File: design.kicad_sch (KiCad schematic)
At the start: 80 parts, among them J1 2601-3108, J10 Conn_01x04, J11 Conn_01x04, J12 Conn_01x03, J13 Conn_01x03, J14 BM04B-SRSS-TB_LF__SN_, J2 2601-3108, J3 2601-3108, J4 TYPE-C-31-M-12, J5 SKEDD-UPDI-4, J6 Conn_01x04, J7 Conn_01x04, J8 Conn_01x04, J9 Conn_01x04, U1 ATtiny1616-S, U2 AP2112K-3.3, U3 CP2105

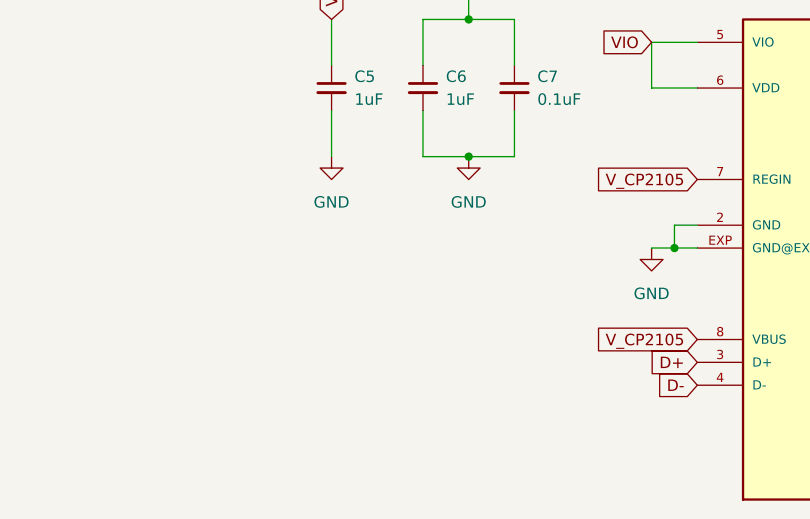
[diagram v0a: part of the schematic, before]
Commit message: add CP2105 VBus solderbridge
closes #5
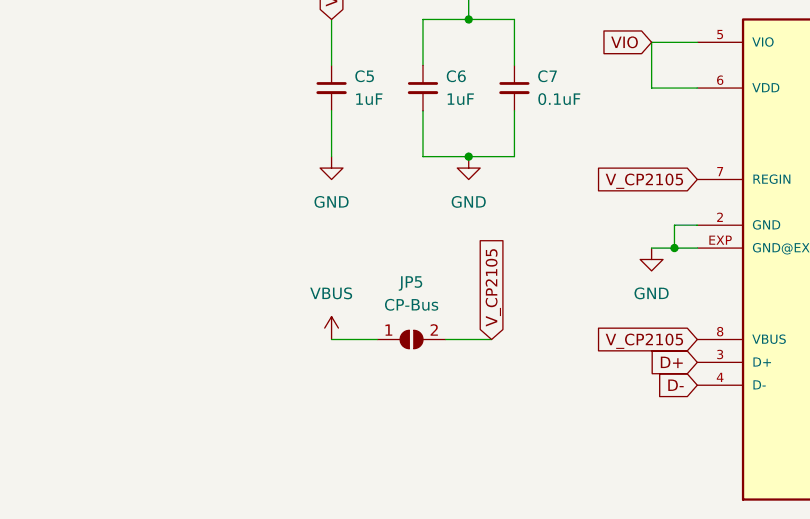
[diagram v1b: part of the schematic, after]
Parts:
- added JP5: CP-Bus, Jumper:SolderJumper-2_P1.3mm_Open_Pad1.0x1.5mm, symbol Jumper:SolderJumper_2_Open
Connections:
- net VBUS: now also JP5.1 (A)
- net V_CP2105: now also JP5.2 (B)
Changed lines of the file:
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@@
     (stroke (width 0) (type default) (color 0 0 0 0))
   )
+  (wire (pts (xy 175.26 248.92) (xy 180.34 248.92))
+    (stroke (width 0) (type default) (color 0 0 0 0))
+  )
   (wire (pts (xy 358.14 185.42) (xy 358.14 180.34))
     (stroke (width 0) (type default) (color 0 0 0 0))
@@
     (stroke (width 0) (type default) (color 0 0 0 0))
   )
+  (wire (pts (xy 162.56 248.92) (xy 167.64 248.92))
+    (stroke (width 0) (type default) (color 0 0 0 0))
+  )
   (wire (pts (xy 28.575 33.02) (xy 33.02 33.02))
     (stroke (width 0) (type default) (color 0 0 0 0))
@@
     )
   )
+  (global_label "V_CP2105" (shape input) (at 180.34 248.92 90) (fields_autoplaced)
+    (effects (font (size 1.27 1.27)) (justify left))
+    (property "Referenzen zwischen Schaltplänen" "${INTERSHEET_REFS}" (id 0) (at 180.2606 237.1615 90)
+      (effects (font (size 1.27 1.27)) (justify left) hide)
+    )
+  )
   (global_label "PB0" (shape input) (at 96.52 150.749 180) (fields_autoplaced)
     (effects (font (size 1.27 1.27)) (justify right))
@@
     (pin "4")
   )
+  (symbol (lib_id "Jumper:SolderJumper_2_Open") (at 171.45 248.92 0) (unit 1)
+    (in_bom yes) (on_board yes) (fields_autoplaced)
+    (property "Reference" "JP5" (id 0) (at 171.45 242.57 0))
+    (property "Value" "CP-Bus" (id 1) (at 171.45 245.11 0))
+    (property "Footprint" "Jumper:SolderJumper-2_P1.3mm_Open_Pad1.0x1.5mm" (id 2) (at 171.45 248.92 0)
+      (effects (font (size 1.27 1.27)) hide)
+    )
+    (property "Datasheet" "~" (id 3) (at 171.45 248.92 0)
+      (effects (font (size 1.27 1.27)) hide)
+    )
+    (pin "1")
+    (pin "2")
+  )
   (symbol (lib_id "power:PWR_FLAG") (at 237.49 154.94 90) (unit 1)
     (in_bom yes) (on_board yes)
@@
     (pin "1")
   )
+  (symbol (lib_id "power:VBUS") (at 162.56 248.92 0) (unit 1)
+    (in_bom yes) (on_board yes) (fields_autoplaced)
+    (property "Reference" "#PWR0106" (id 0) (at 162.56 252.73 0)
+      (effects (font (size 1.27 1.27)) hide)
+    )
+    (property "Value" "VBUS" (id 1) (at 162.56 243.84 0))
+    (property "Footprint" "" (id 2) (at 162.56 248.92 0)
+      (effects (font (size 1.27 1.27)) hide)
+    )
+    (property "Datasheet" "" (id 3) (at 162.56 248.92 0)
+      (effects (font (size 1.27 1.27)) hide)
+    )
+    (pin "1")
+  )
   (symbol (lib_id "power:VBUS") (at 167.64 157.48 0) (mirror y) (unit 1)
     (in_bom yes) (on_board yes)
@@
       (reference "#PWR0105") (unit 1) (value "VCC") (footprint "")
     )
+    (path "/528fa40b-d5ff-4783-ba33-55bca0f34b24"
+      (reference "#PWR0106") (unit 1) (value "VBUS") (footprint "")
+    )
     (path "/c097fc70-84bb-4a84-8a27-d6457ac14a2c"
       (reference "#PWR0107") (unit 1) (value "GND") (footprint "")
@@
       (reference "JP4") (unit 1) (value "LED2x2") (footprint "Jumper:SolderJumper-2_P1.3mm_Open_Pad1.0x1.5mm")
     )
+    (path "/14405b68-8ab5-4c92-8056-b559eb773953"
+      (reference "JP5") (unit 1) (value "CP-Bus") (footprint "Jumper:SolderJumper-2_P1.3mm_Open_Pad1.0x1.5mm")
+    )
     (path "/be5d4d29-c7d2-4c92-a91e-3f85187a2fa5"

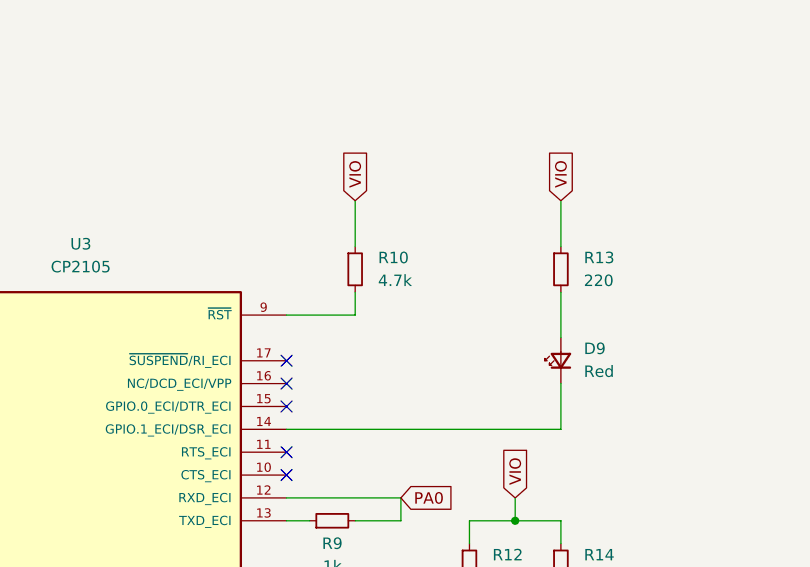
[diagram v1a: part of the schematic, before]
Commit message: add programming capacitor
closes #4
to use the TX/RX LEDs the cp2105 must be programmed to use this function (only one time possible). Todo this a 4,7uF capacitor must be used on pin VPP according to the Datasheet Note 4 page 18.
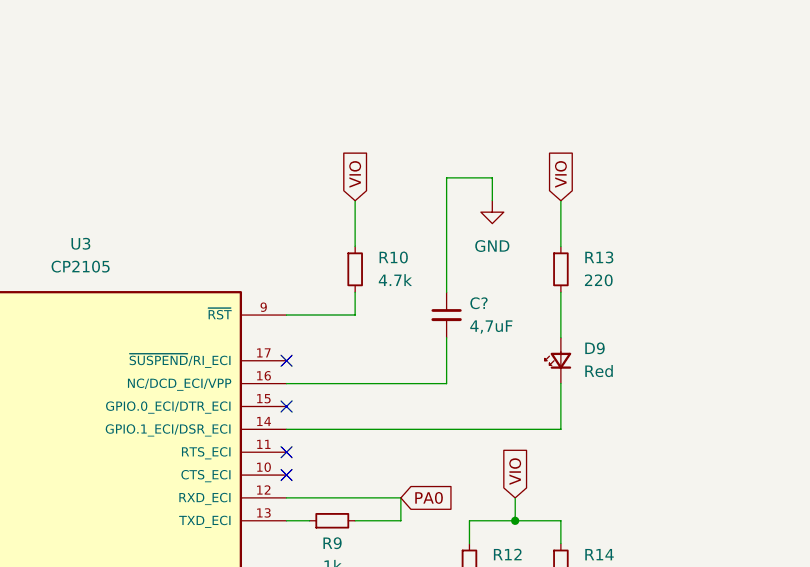
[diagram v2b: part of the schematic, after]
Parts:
- added C?: 4,7uF, Capacitor_SMD:C_0805_2012Metric, symbol Device:C_Small
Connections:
- net GND: now also C?.1
- net at U3.16 (NC/DCD_ECI/VPP): now also C?.2
- no-connect marks 14 -> 13
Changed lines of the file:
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@@
   )
   (no_connect (at 248.92 220.98))
-  (no_connect (at 248.92 223.52))
   (no_connect (at 248.92 233.68))
   (no_connect (at 68.58 45.72))
@@
     (stroke (width 0) (type default) (color 0 0 0 0))
   )
+  (wire (pts (xy 266.7 200.66) (xy 266.7 213.36))
+    (stroke (width 0) (type default) (color 0 0 0 0))
+  )
   (wire (pts (xy 71.12 182.88) (xy 71.12 180.34))
     (stroke (width 0) (type default) (color 0 0 0 0))
@@
     (stroke (width 0) (type default) (color 0 0 0 0))
   )
+  (wire (pts (xy 266.7 223.52) (xy 266.7 218.44))
+    (stroke (width 0) (type default) (color 0 0 0 0))
+  )
   (wire (pts (xy 358.14 205.74) (xy 358.14 200.66))
     (stroke (width 0) (type default) (color 0 0 0 0))
@@
     (stroke (width 0) (type default) (color 0 0 0 0))
   )
+  (wire (pts (xy 271.78 200.66) (xy 266.7 200.66))
+    (stroke (width 0) (type default) (color 0 0 0 0))
+  )
   (wire (pts (xy 322.58 144.78) (xy 325.12 144.78))
     (stroke (width 0) (type default) (color 0 0 0 0))
@@
     (stroke (width 0) (type default) (color 0 0 0 0))
   )
+  (wire (pts (xy 248.92 223.52) (xy 266.7 223.52))
+    (stroke (width 0) (type default) (color 0 0 0 0))
+  )
   (wire (pts (xy 172.085 40.64) (xy 180.34 40.64))
     (stroke (width 0) (type default) (color 0 0 0 0))
@@
     (stroke (width 0) (type default) (color 0 0 0 0))
   )
+  (wire (pts (xy 271.78 203.2) (xy 271.78 200.66))
+    (stroke (width 0) (type default) (color 0 0 0 0))
+  )
   (wire (pts (xy 353.06 139.7) (xy 353.06 137.16))
     (stroke (width 0) (type default) (color 0 0 0 0))
@@
     (pin "1")
   )
+  (symbol (lib_id "power:GND") (at 271.78 203.2 0) (unit 1)
+    (in_bom yes) (on_board yes) (fields_autoplaced)
+    (property "Reference" "#PWR?" (id 0) (at 271.78 209.55 0)
+      (effects (font (size 1.27 1.27)) hide)
+    )
+    (property "Value" "GND" (id 1) (at 271.78 208.28 0))
+    (property "Footprint" "" (id 2) (at 271.78 203.2 0)
+      (effects (font (size 1.27 1.27)) hide)
+    )
+    (property "Datasheet" "" (id 3) (at 271.78 203.2 0)
+      (effects (font (size 1.27 1.27)) hide)
+    )
+    (pin "1")
+  )
   (symbol (lib_id "power:VDD") (at 355.6 83.82 0) (mirror y) (unit 1)
     (in_bom yes) (on_board yes)
@@
     (pin "1")
   )
+  (symbol (lib_id "Device:C_Small") (at 266.7 215.9 0) (unit 1)
+    (in_bom yes) (on_board yes) (fields_autoplaced)
+    (property "Reference" "C?" (id 0) (at 269.24 214.6362 0)
+      (effects (font (size 1.27 1.27)) (justify left))
+    )
+    (property "Value" "4,7uF" (id 1) (at 269.24 217.1762 0)
+      (effects (font (size 1.27 1.27)) (justify left))
+    )
+    (property "Footprint" "Capacitor_SMD:C_0805_2012Metric" (id 2) (at 266.7 215.9 0)
+      (effects (font (size 1.27 1.27)) hide)
+    )
+    (property "Datasheet" "~" (id 3) (at 266.7 215.9 0)
+      (effects (font (size 1.27 1.27)) hide)
+    )
+    (pin "1")
+    (pin "2")
+  )
   (symbol (lib_id "power:GND") (at 18.796 170.18 0) (unit 1)
     (in_bom yes) (on_board yes)
@@
       (reference "#PWR0189") (unit 1) (value "GND") (footprint "")
     )
+    (path "/cc5fd905-24ad-457d-947c-2c2437ded00b"
+      (reference "#PWR?") (unit 1) (value "GND") (footprint "")
+    )
     (path "/5005112b-a25c-4019-a0f7-bec67dd371e4"
       (reference "C1") (unit 1) (value "1uF") (footprint "Capacitor_SMD:C_0805_2012Metric")
@@
       (reference "C7") (unit 1) (value "0.1uF") (footprint "Capacitor_SMD:C_0805_2012Metric")
     )
+    (path "/d80388e9-556a-442b-9d58-9f39d8934e6e"
+      (reference "C?") (unit 1) (value "4,7uF") (footprint "Capacitor_SMD:C_0805_2012Metric")
+    )
     (path "/5ec38a02-a145-4acb-a554-76dbb10c2abb"

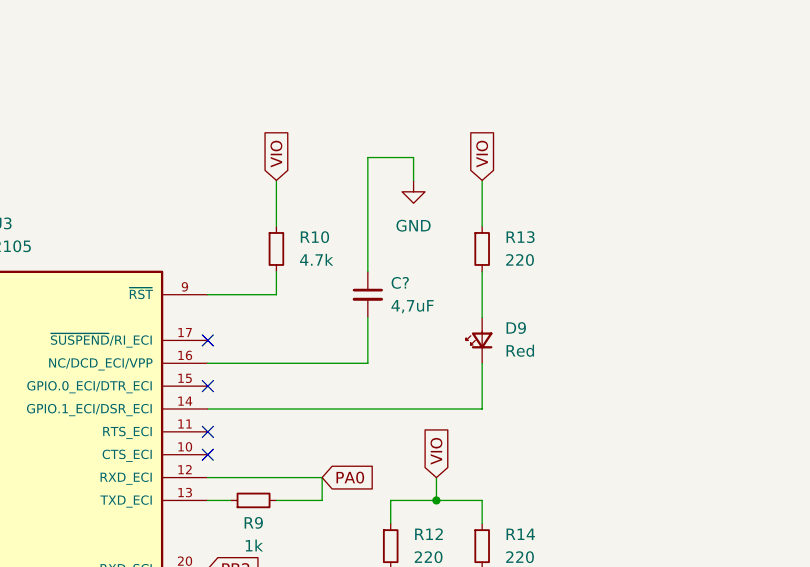
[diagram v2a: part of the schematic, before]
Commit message: add designators
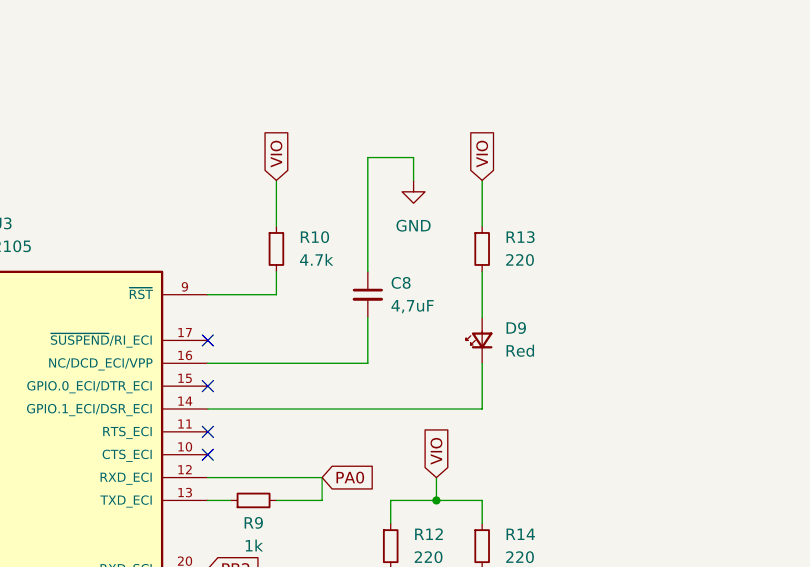
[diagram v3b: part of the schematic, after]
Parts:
- gave numbers to parts that had none: 1
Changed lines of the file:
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@@
   (symbol (lib_id "power:GND") (at 271.78 203.2 0) (unit 1)
     (in_bom yes) (on_board yes) (fields_autoplaced)
-    (property "Reference" "#PWR?" (id 0) (at 271.78 209.55 0)
+    (property "Reference" "#PWR0190" (id 0) (at 271.78 209.55 0)
       (effects (font (size 1.27 1.27)) hide)
     )
@@
   (symbol (lib_id "Device:C_Small") (at 266.7 215.9 0) (unit 1)
     (in_bom yes) (on_board yes) (fields_autoplaced)
-    (property "Reference" "C?" (id 0) (at 269.24 214.6362 0)
+    (property "Reference" "C8" (id 0) (at 269.24 214.6362 0)
       (effects (font (size 1.27 1.27)) (justify left))
     )
@@
     )
     (path "/cc5fd905-24ad-457d-947c-2c2437ded00b"
-      (reference "#PWR?") (unit 1) (value "GND") (footprint "")
+      (reference "#PWR0190") (unit 1) (value "GND") (footprint "")
     )
     (path "/5005112b-a25c-4019-a0f7-bec67dd371e4"
@@
     )
     (path "/d80388e9-556a-442b-9d58-9f39d8934e6e"
-      (reference "C?") (unit 1) (value "4,7uF") (footprint "Capacitor_SMD:C_0805_2012Metric")
+      (reference "C8") (unit 1) (value "4,7uF") (footprint "Capacitor_SMD:C_0805_2012Metric")
     )
     (path "/5ec38a02-a145-4acb-a554-76dbb10c2abb"

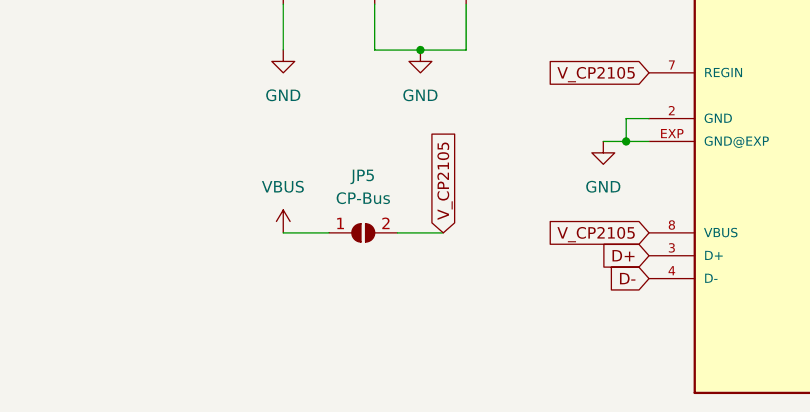
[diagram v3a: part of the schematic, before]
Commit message: add note for jp5
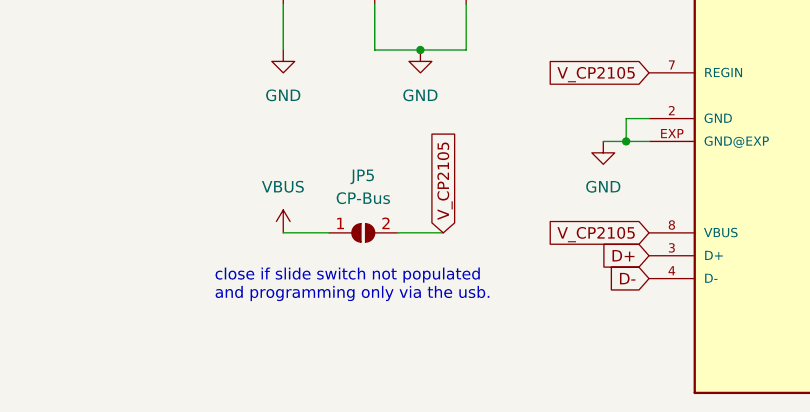
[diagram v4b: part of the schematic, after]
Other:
- note added: "close if slide switch not populated and programming only via the usb."
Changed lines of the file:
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@@
+    (effects (font (size 1.27 1.27)) (justify left bottom))
+  )
+  (text "close if slide switch not populated \nand programming only via the usb."
+    (at 154.94 256.54 0)
     (effects (font (size 1.27 1.27)) (justify left bottom))
   )
